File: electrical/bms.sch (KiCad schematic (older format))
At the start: 34 parts, among them Q1 Q_PMOS_DGS, Q2 Q_NMOS_DGS, Q3 Q_PMOS_DGS, Q4 Q_PMOS_DGS

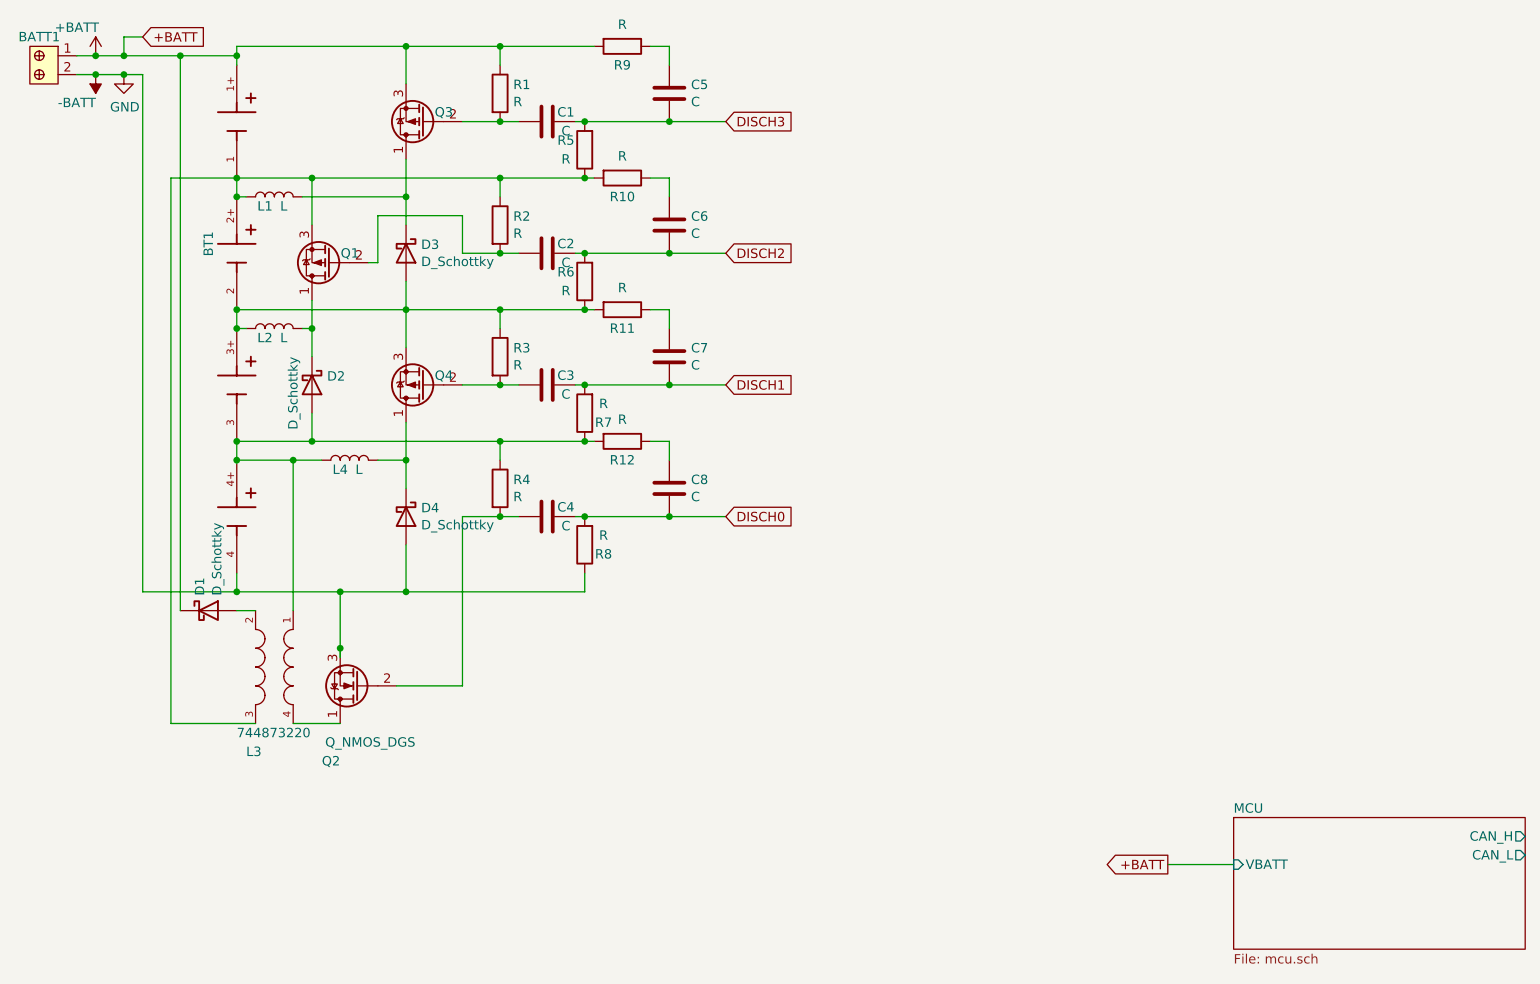
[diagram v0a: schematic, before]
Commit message: Moved batteries to own sheet
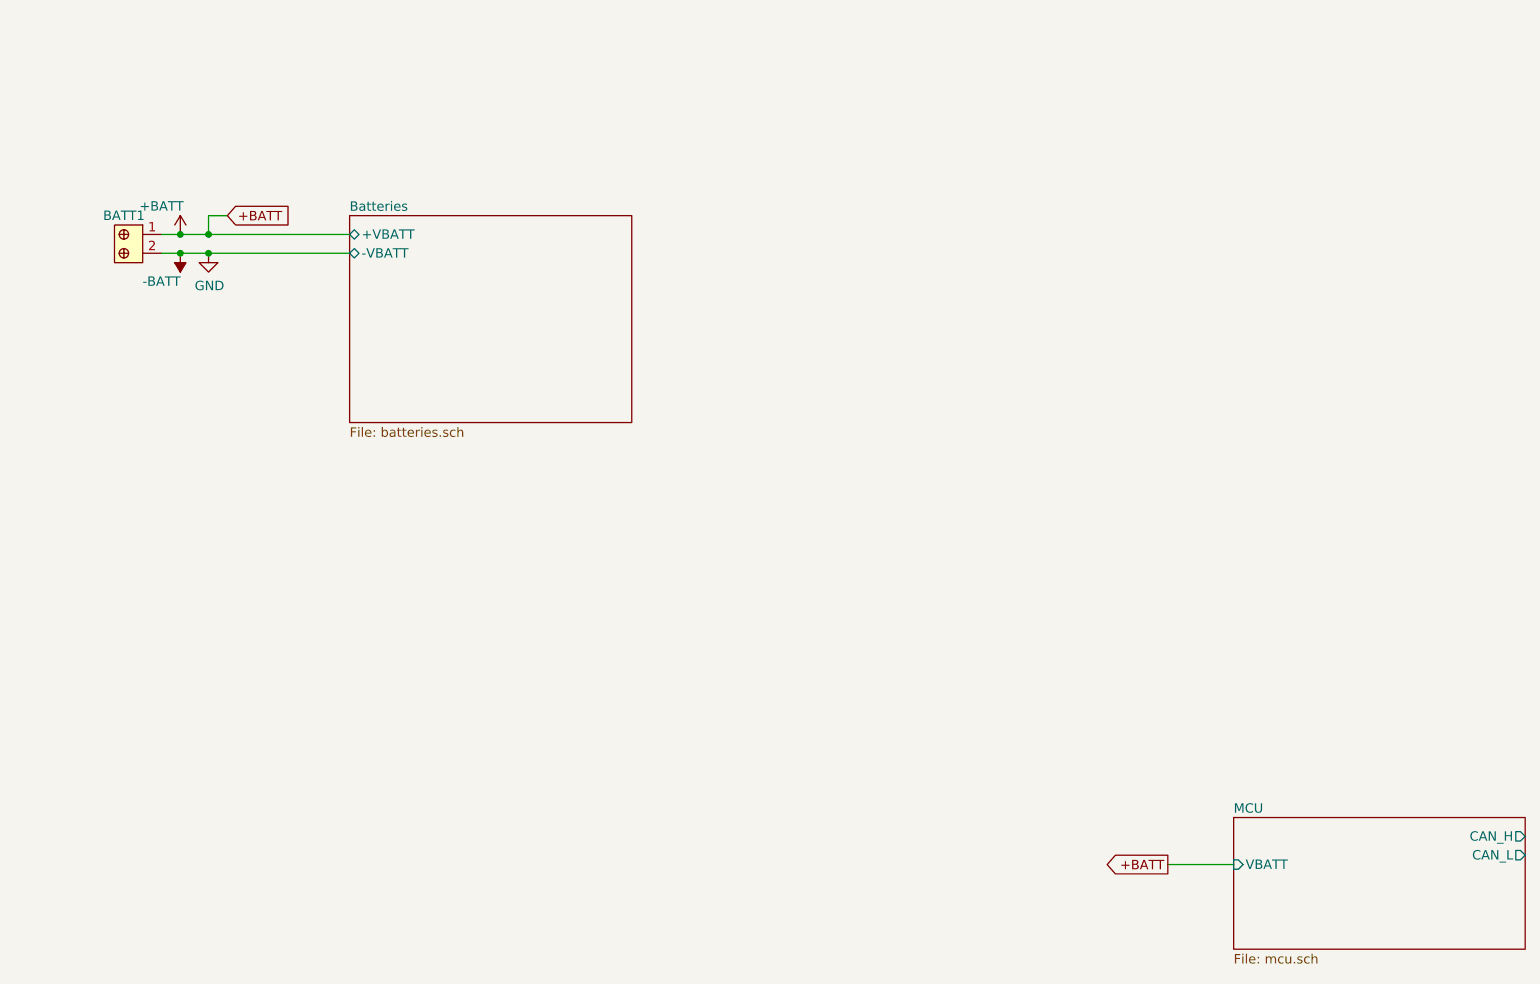
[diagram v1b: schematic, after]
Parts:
- removed BT1: BK-18650-PC8, BAT_BK-18650-PC8, symbol BK-18650-PC8:BK-18650-PC8
- removed C1, C2, C3, C4, C5, C6, C7, C8: C, symbol Device:C
- removed D1, D2, D3, D4: D_Schottky, symbol Device:D_Schottky
- removed L1, L2, L4: L, symbol Device:L
- removed L3: 744873220, WU744873220:Wurth_Electronics-744873220-Manufacturer_Recommended, symbol WU744873220:744873220
- removed Q1, Q3, Q4: Q_PMOS_DGS, symbol Device:Q_PMOS_DGS
- removed Q2: Q_NMOS_DGS, symbol Device:Q_NMOS_DGS
- removed R1, R10, R11, R12, R2, R3, R4, R5, R6, R7, R8, R9: R, symbol Device:R
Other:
- moved on the sheet: BATT1
